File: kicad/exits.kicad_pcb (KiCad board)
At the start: 2 copper layers, 39.3 x 106.5 mm, 54 parts, among them J1 PJ301M12, J12 Euro power header, J13 PJ301M12, J14 PJ301M12, J2 PJ301M12, J3 PJ301M12, J4 PJ301M12, J5 Attenuator Jumper 1, J6 Attenuator Jumper 2, U1 TL074, U2 RC4580

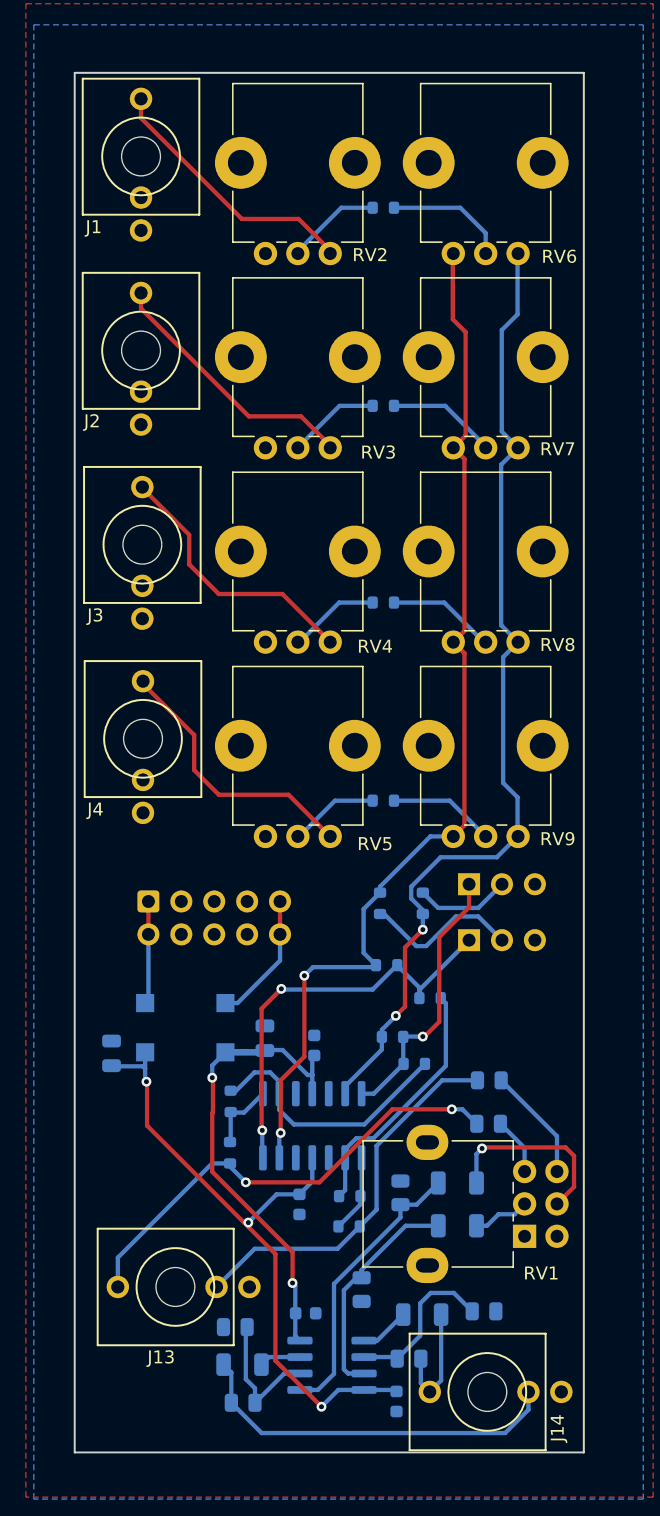
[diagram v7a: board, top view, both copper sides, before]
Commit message: Switched L and R channels, so pots all turn the right way
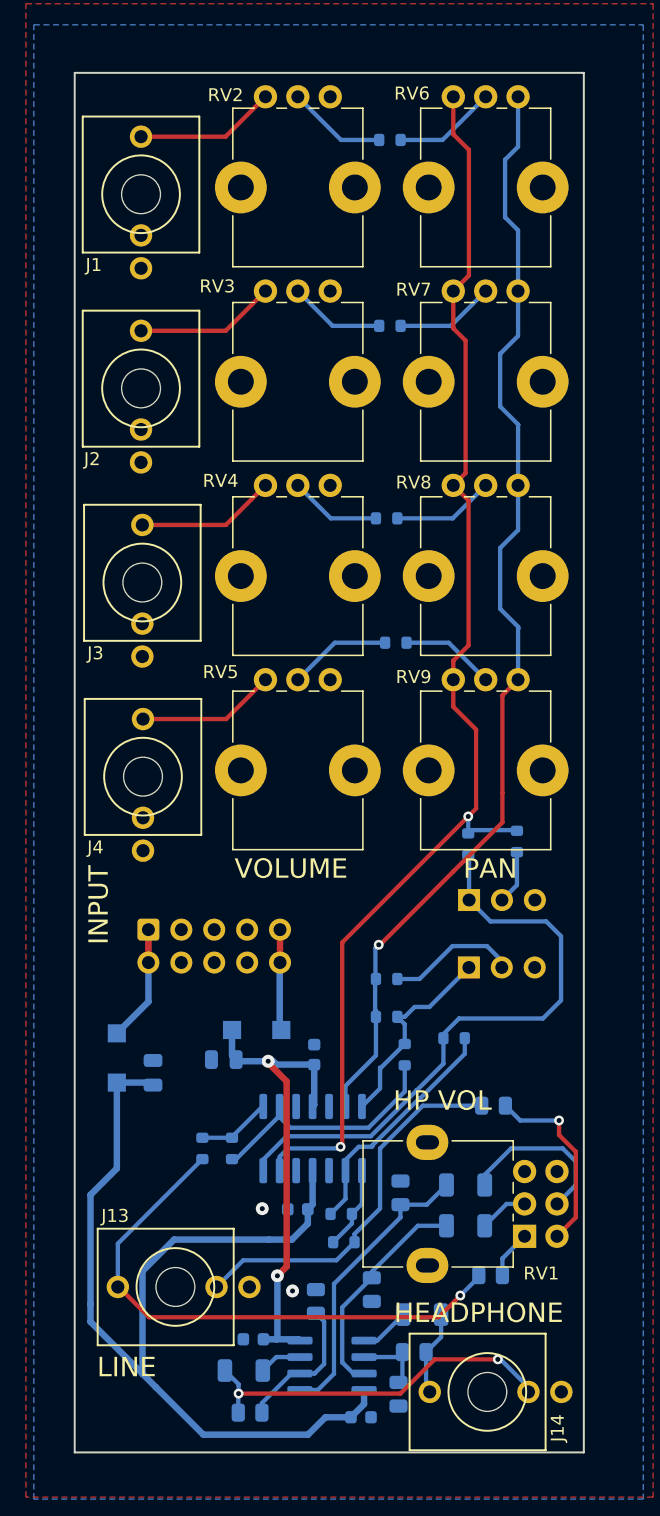
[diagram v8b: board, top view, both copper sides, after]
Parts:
- moved RV2 13.1 mm to (29.0, 27.4), turned to -90 degrees
- moved RV3 13.1 mm to (29.0, 42.4), turned to -90 degrees
- moved RV4 13.1 mm to (29.0, 57.4), turned to -90 degrees
- moved RV6 13.1 mm to (43.5, 27.4), turned to -90 degrees
- moved RV7 13.1 mm to (43.5, 42.4), turned to -90 degrees
- moved RV8 13.1 mm to (43.5, 57.4), turned to -90 degrees
- moved RV5 13.1 mm to (29.0, 72.4), turned to -90 degrees
- moved RV9 13.1 mm to (43.5, 72.4), turned to -90 degrees
- moved R7 12.2 mm to (39.1, 69.5)
- moved R35 11.7 mm to (46.4, 118.4)
- moved R19 11.6 mm to (48.4, 84.9)
- moved R20 11.3 mm to (44.7, 85.1), turned to -90 degrees
- moved R23 9.20 mm to (39.3, 127.6), turned to 90 degrees
- moved R24 6.53 mm to (32.9, 120.4), turned to -90 degrees
- moved R5 6.51 mm to (38.4, 59.9)
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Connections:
- RV1 pad 1: GND -> Net-(R35-Pad1)
- RV1 pad 3: Net-(R35-Pad1) -> GND
- RV1 pad 4: GND -> Net-(R36-Pad1)
- RV1 pad 6: Net-(R36-Pad1) -> GND
- RV6 pad 1: /LeftMix -> /RightMix
- RV6 pad 3: /RightMix -> /LeftMix
- RV7 pad 1: /LeftMix -> /RightMix
- RV7 pad 3: /RightMix -> /LeftMix
- RV8 pad 1: /LeftMix -> /RightMix
- RV8 pad 3: /RightMix -> /LeftMix
- RV9 pad 1: /LeftMix -> /RightMix
- RV9 pad 3: /RightMix -> /LeftMix
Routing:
- net -12V: track 50.2 -> 75.4 mm, vias 3 -> 0
- net /RightMix: track 82.0 -> 100.2 mm
- net Net-(J6-Pad1): track 33.3 -> 47.0 mm, vias 2 -> 0
- net /LeftMix: track 76.1 -> 86.8 mm, vias 2 -> 1
- net Net-(J4-Pad3): track 21.1 -> 10.7 mm
- net Net-(J3-Pad3): track 20.8 -> 10.8 mm
- net Net-(J1-Pad3): track 20.6 -> 10.9 mm
- net Net-(J2-Pad3): track 20.4 -> 10.9 mm
- net Net-(J6-Pad2): track 12.1 -> 4.17 mm
- net Net-(R23-Pad2): track 12.4 -> 5.59 mm
- net LLineOut: track 36.5 -> 42.8 mm, vias 2 -> 1
- net Net-(R36-Pad1): track 8.83 -> 14.7 mm, vias 0 -> 1
- net Net-(J5-Pad1): track 21.1 -> 15.7 mm, vias 1 -> 0
- net Net-(J5-Pad2): track 7.36 -> 10.1 mm
- net HPoutL: track 9.18 -> 6.57 mm
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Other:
- board text added: "2/3 GAIN"
- board text added: "3 2 1"
- board text added: "<-"
- board text added: "CC BY-SA 4.0"
- board text added: "GAIN"
- board text added: "HEADPHONE"
- board text added: "HP VOL"
- board text added: "INPUT"
- board text added: "LINE"
- board text added: "PAN"
- board text added: "VOLUME"
- board text removed: "<- CC BY-SA 4.0"
